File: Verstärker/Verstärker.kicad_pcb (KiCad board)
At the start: 2 copper layers, 137.5 x 53 mm, 63 parts, among them J3 ACJS-MHOM, J4 NRJ6HM-1, Q1 MJE182G, Q12 MMBT5401, Q12&Q13_E TP9, Q12_B TP4, Q12_C TP10, Q13 MMBT5401, Q13&Q12_C TP11, Q13_E TP8, Q1_E TP2, Q2 MJE172G, Q2_E TP3, Q3 MMBT5551(RANGE:200-300), Q3_C TP6, Q3_E TP7, Q9 MMBT5551(RANGE:200-300)

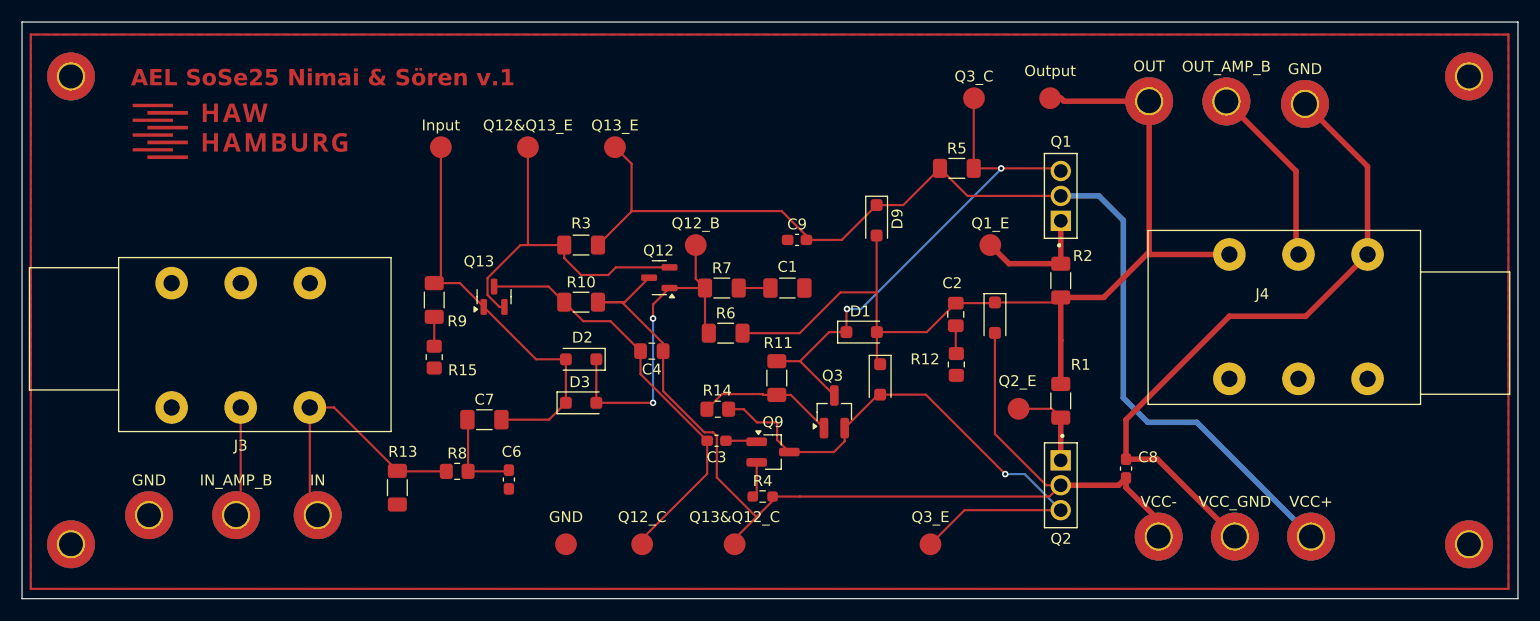
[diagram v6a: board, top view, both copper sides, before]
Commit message: Alles auf 10cm Breite geschrumpft. Keine Vias
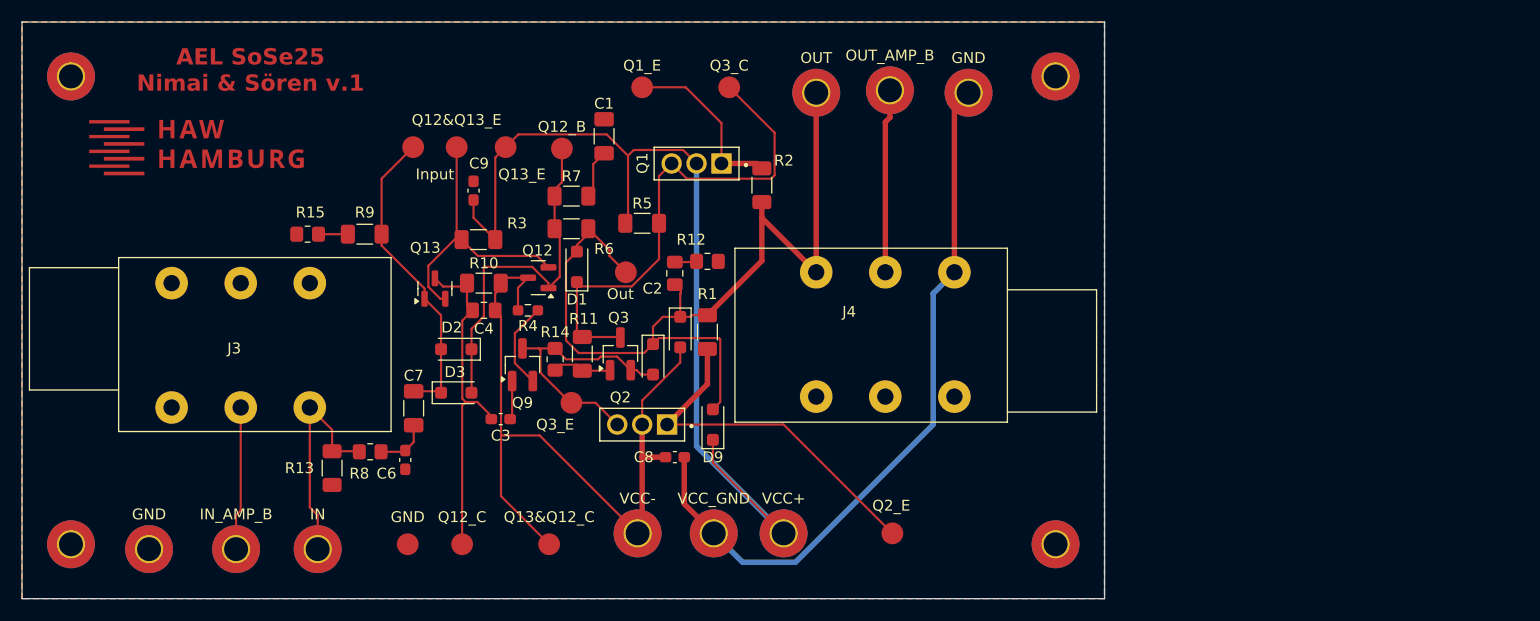
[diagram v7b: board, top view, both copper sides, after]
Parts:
- moved VCC+ 48.5 mm to (107.0, 106.0)
- moved VCC- 47.9 mm to (93.6, 106.0)
- moved VCC_GND 47.9 mm to (100.6, 106.0)
- moved Out 42.2 mm to (92.5, 82.0)
- moved C8 41.5 mm to (97.0, 99.0), turned to 180 degrees
- moved J4 38.0 mm to (110.0, 82.0)
- moved GND6 38.0 mm to (132.0, 64.0)
- moved GND7 38.0 mm to (132.0, 107.0)
- moved Q2 36.3 mm to (96.3, 96.0), turned to 180 degrees
- moved Q3_E 35.5 mm to (87.5, 94.0)
- moved Q1_E 35.1 mm to (94.0, 65.0)
- moved R1 33.1 mm to (100.0, 87.5)
- moved Q1 31.6 mm to (101.3, 72.0), turned to 180 degrees
- moved GND 30.9 mm to (124.0, 65.5)
- moved OUT_AMP_B 30.9 mm to (116.8, 65.3)
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- renumbered Output to Out
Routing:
- net Net-(D4-A): track 53.8 -> 24.5 mm, vias 1 -> 0
- net Net-(D10-A): track 95.8 -> 69.6 mm
- net Net-(Q2-E): track 8.14 -> 33.3 mm
- net Net-(D9-K): track 101.0 -> 87.9 mm
- net Net-(D2-A): track 38.3 -> 28.7 mm
- net Net-(Q3-B): track 12.6 -> 5.51 mm
- net Net-(Q12-E): track 32.7 -> 25.7 mm
- net Net-(Q13-C): track 38.2 -> 31.4 mm
- net Net-(D1-A): track 92.8 -> 86.2 mm
- net GND: track 61.3 -> 66.5 mm
- net Net-(Q1-E): track 11.1 -> 16.3 mm
- net Net-(Q9-E): track 3.29 -> 8.06 mm
- net Net-(IN1-Pad1): track 25.2 -> 20.7 mm
- net Net-(C6-Pad2): track 8.57 -> 4.92 mm
- net Net-(IN_AMP_B1-Pad1): track 10.1 -> 13.2 mm
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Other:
- board size 137.5 x 53 mm -> 99.5 x 53 mm

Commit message: Erste Korrektur Revesion
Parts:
- moved Q12&Q13_E 7.17 mm to (78.5, 63.5)
- moved Q13_E 7.17 mm to (83.0, 63.5)
- moved Input 7.02 mm to (73.5, 63.5)
- moved Q3_C 2.92 mm to (99.5, 63.5)
- moved Q1_E 1.50 mm to (94.0, 63.5)
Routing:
- net Net-(Q12-E): track 25.7 -> 33.4 mm
- net Net-(D2-A): track 28.7 -> 35.9 mm
- net Net-(D9-K): track 87.9 -> 93.3 mm
- net Net-(D1-K): track 46.8 -> 49.3 mm
- net Net-(D1-A): track 86.2 -> 84.5 mm
- net Net-(Q1-E): track 16.3 -> 15.4 mm
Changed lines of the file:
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@@
 	(footprint "TestPoint:TestPoint_Pad_D2.0mm"
 		(layer "F.Cu")
-		(at 72.95 70.5)
+		(at 73.5 63.5)
 		(descr "SMD pad as test Point, diameter 2.0mm")
 		(tags "test point SMD pad")
@@
 	(footprint "TestPoint:TestPoint_Pad_D2.0mm"
 		(layer "F.Cu")
-		(at 94 65)
+		(at 94 63.5)
 		(descr "SMD pad as test Point, diameter 2.0mm")
 		(tags "test point SMD pad")
@@
 	(footprint "TestPoint:TestPoint_Pad_D2.0mm"
 		(layer "F.Cu")
-		(at 76.95 70.5)
+		(at 78.5 63.5)
 		(descr "SMD pad as test Point, diameter 2.0mm")
 		(tags "test point SMD pad")
@@
 	(footprint "TestPoint:TestPoint_Pad_D2.0mm"
 		(layer "F.Cu")
-		(at 81.45 70.5)
+		(at 83 63.5)
 		(descr "SMD pad as test Point, diameter 2.0mm")
 		(tags "test point SMD pad")
@@
 	(footprint "TestPoint:TestPoint_Pad_D2.0mm"
 		(layer "F.Cu")
-		(at 102 65)
+		(at 99.5 63.5)
 		(descr "SMD pad as test Point, diameter 2.0mm")
 		(tags "test point SMD pad")
@@
 	)
 	(segment
-		(start 110 82)
-		(end 105 77)
-		(width 0.5)
-		(layer "F.Cu")
-		(net 4)
-	)
-	(segment
 		(start 105 77)
 		(end 105 80.95)
@@
 	)
 	(segment
+		(start 105 80.95)
+		(end 107.95 80.95)
+		(width 0.5)
+		(layer "F.Cu")
+		(net 4)
+	)
+	(segment
 		(start 89.05 78.45)
 		(end 88 79.5)
@@
 	)
 	(segment
+		(start 109 82)
+		(end 110 82)
+		(width 0.5)
+		(layer "F.Cu")
+		(net 4)
+	)
+	(segment
 		(start 97 83.1375)
 		(end 97.55 83.6875)
@@
 	)
 	(segment
+		(start 107.95 80.95)
+		(end 109 82)
+		(width 0.5)
+		(layer "F.Cu")
+		(net 4)
+	)
+	(segment
 		(start 91 79.95)
 		(end 89.05 78)
@@
 	)
 	(segment
+		(start 73.5 69.95)
+		(end 73.5 63.5)
+		(width 0.2)
+		(layer "F.Cu")
+		(net 9)
+	)
+	(segment
+		(start 70.05 78.5)
+		(end 70.05 73.4)
+		(width 0.2)
+		(layer "F.Cu")
+		(net 9)
+	)
+	(segment
 		(start 75.515057 89.074827)
 		(end 75.515057 85.952557)
@@
 	)
 	(segment
-		(start 70.05 78.5)
-		(end 70.05 73.4)
+		(start 70.05 73.4)
+		(end 73.5 69.95)
 		(width 0.2)
 		(layer "F.Cu")
@@
 	)
 	(segment
-		(start 70.05 73.4)
-		(end 72.95 70.5)
+		(start 84.174369 69.325631)
+		(end 84.174369 64.674369)
 		(width 0.2)
 		(layer "F.Cu")
-		(net 9)
+		(net 10)
 	)
 	(segment
-		(start 80.5 79)
-		(end 80.5 71.45)
+		(start 100.5 97.4)
+		(end 100.5 99.5)
 		(width 0.2)
 		(layer "F.Cu")
@@
 	)
 	(segment
-		(start 100.5 97.4)
-		(end 100.5 99.5)
+		(start 84.174369 64.674369)
+		(end 83 63.5)
 		(width 0.2)
 		(layer "F.Cu")
@@
 	)
 	(segment
-		(start 90.736791 69.325631)
-		(end 82.624369 69.325631)
+		(start 100.5 99.5)
+		(end 107 106)
 		(width 0.2)
 		(layer "F.Cu")
@@
 	)
 	(segment
-		(start 92.701 71.28984)
-		(end 90.736791 69.325631)
+		(start 93.22934 70.7615)
+		(end 97.7615 70.7615)
 		(width 0.2)
 		(layer "F.Cu")
@@
 	)
 	(segment
-		(start 100.5 99.5)
-		(end 107 106)
+		(start 92.701 71.28984)
+		(end 90.736791 69.325631)
 		(width 0.2)
 		(layer "F.Cu")
@@
 	)
 	(segment
-		(start 93.22934 70.7615)
-		(end 97.7615 70.7615)
+		(start 80.5 73)
+		(end 80.5 79)
 		(width 0.2)
 		(layer "F.Cu")
@@
 	)
 	(segment
-		(start 82.624369 69.325631)
-		(end 81.45 70.5)
+		(start 84.174369 69.325631)
+		(end 80.5 73)
 		(width 0.2)
 		(layer "F.Cu")
@@
 	)
 	(segment
-		(start 92.701 77.249)
-		(end 92.701 71.28984)
+		(start 90.736791 69.325631)
+		(end 84.174369 69.325631)
 		(width 0.2)
 		(layer "F.Cu")
@@
 	)
 	(segment
-		(start 80.5 71.45)
-		(end 81.45 70.5)
+		(start 92.701 77.249)
+		(end 92.701 71.28984)
 		(width 0.2)
 		(layer "F.Cu")
@@
 	)
 	(segment
-		(start 98.111 73.401)
-		(end 105.86016 73.401)
+		(start 93.038892 83.301)
+		(end 88.401 83.301)
 		(width 0.2)
 		(layer "F.Cu")
@@
 	)
 	(segment
-		(start 93.038892 83.301)
-		(end 88.401 83.301)
+		(start 105.86016 73.401)
+		(end 106.176 73.08516)
 		(width 0.2)
 		(layer "F.Cu")
@@
 	)
 	(segment
-		(start 88.5 87.95)
-		(end 91.95 87.95)
+		(start 98.111 73.401)
+		(end 105.86016 73.401)
 		(width 0.2)
 		(layer "F.Cu")
@@
 	)
 	(segment
-		(start 91.95 87.95)
-		(end 92 88)
+		(start 88.5 87.95)
+		(end 91.95 87.95)
 		(width 0.2)
 		(layer "F.Cu")
@@
 	)
 	(segment
-		(start 95.55 77.5)
-		(end 95.55 73.16)
+		(start 91.95 87.95)
+		(end 92 88)
 		(width 0.2)
 		(layer "F.Cu")
@@
 	)
 	(segment
-		(start 105.86016 73.401)
-		(end 106.176 73.08516)
+		(start 106.176 73.08516)
+		(end 106.176 70.176)
 		(width 0.2)
 		(layer "F.Cu")
@@
 	)
 	(segment
-		(start 96.71 72)
-		(end 98.111 73.401)
+		(start 95.55 77.5)
+		(end 95.55 73.16)
 		(width 0.2)
 		(layer "F.Cu")
@@
 	)
 	(segment
-		(start 106.176 73.08516)
-		(end 106.176 69.176)
+		(start 106.176 70.176)
+		(end 99.5 63.5)
 		(width 0.2)
 		(layer "F.Cu")
@@
 	)
 	(segment
-		(start 106.176 69.176)
-		(end 102 65)
+		(start 88 82.9)
+		(end 88 87.45)
 		(width 0.2)
 		(layer "F.Cu")
@@
 	)
 	(segment
-		(start 88 82.9)
-		(end 88 87.45)
+		(start 96.71 72)
+		(end 98.111 73.401)
 		(width 0.2)
 		(layer "F.Cu")
@@
 	)
 	(segment
-		(start 94 65)
-		(end 98 65)
-		(width 0.2)
-		(layer "F.Cu")
-		(net 23)
-	)
-	(segment
-		(start 101.29 68.29)
+		(start 101.29 70.79)
 		(end 101.29 72)
 		(width 0.2)
@@
 	)
 	(segment
-		(start 98 65)
-		(end 101.29 68.29)
+		(start 94 63.5)
+		(end 101.29 70.79)
 		(width 0.2)
 		(layer "F.Cu")
@@
 	)
 	(segment
-		(start 76.95 70.5)
-		(end 76.95 78.55)
-		(width 0.2)
-		(layer "F.Cu")
-		(net 27)
-	)
-	(segment
 		(start 75.9 84.4375)
 		(end 75.445532 84.4375)
@@
 		(width 0.2)
 		(layer "F.Cu")
+		(net 27)
+	)
+	(segment
+		(start 77 67.5)
+		(end 77 65)
+		(width 0.2)
+		(layer "F.Cu")
+		(net 27)
+	)
+	(segment
+		(start 77 67.5)
+		(end 76.95 67.55)
+		(width 0.2)
+		(layer "F.Cu")
+		(net 27)
+	)
+	(segment
+		(start 76.95 67.55)
+		(end 76.95 78.55)
+		(width 0.2)
+		(layer "F.Cu")
+		(net 27)
+	)
+	(segment
+		(start 77 65)
+		(end 78.5 63.5)
+		(width 0.2)
+		(layer "F.Cu")
